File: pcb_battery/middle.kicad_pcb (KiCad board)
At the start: 2 copper layers, 100 x 29.9 mm, 7 parts, among them J1 BAT+, J2 BAT-, J3 TOP+, J4 BOT+, J5 TOP-, J6 BOT-

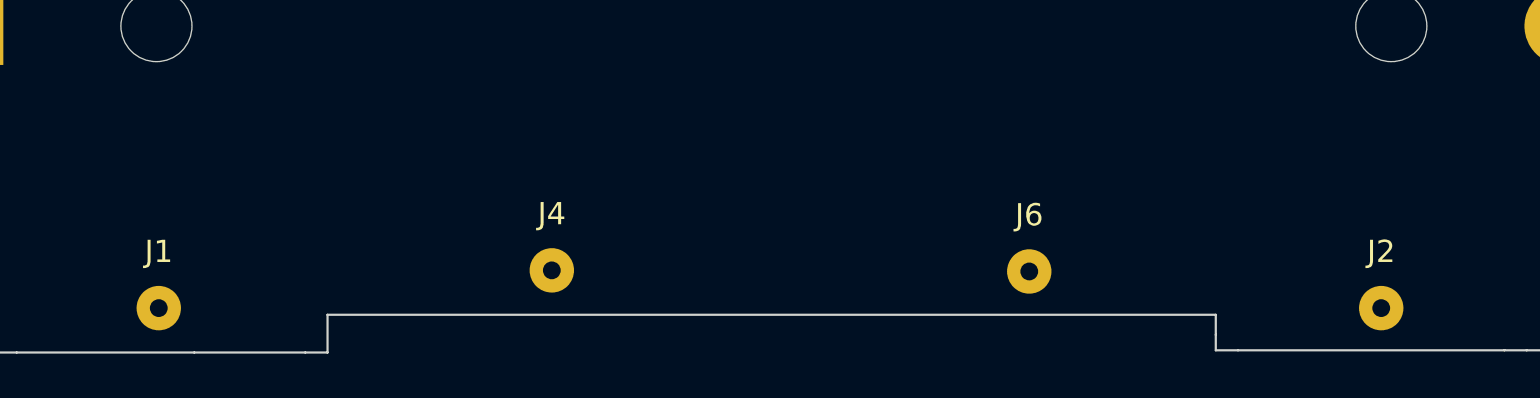
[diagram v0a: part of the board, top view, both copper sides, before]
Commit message: Add the bottom pcb.
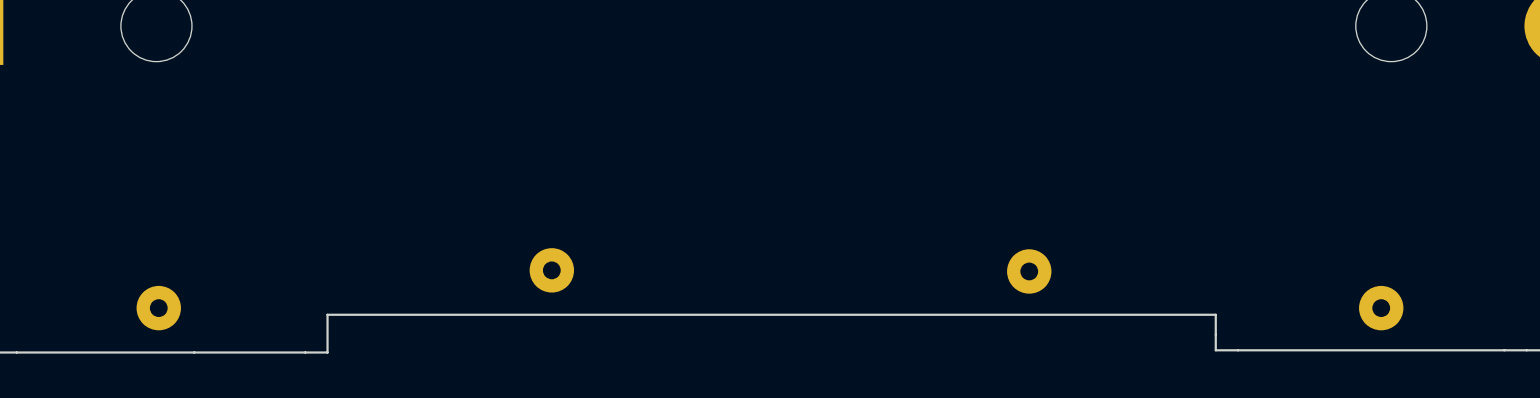
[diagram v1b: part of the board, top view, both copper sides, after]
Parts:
- J1, J2, J4, J6: moved to B.Cu
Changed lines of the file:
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@@
     (add_net "Net-(J5-Pad1)")
   )
-  (module Connector_Wire:SolderWirePad_1x01_Drill0.8mm (layer F.Cu)
+  (module Connector_Wire:SolderWirePad_1x01_Drill0.8mm (layer B.Cu)
     (at 11.6 -18.35)
     (descr "Wire solder connection")
     (tags connector)
     (attr virtual)
-    (fp_text reference J6 (at 0 -2.54) (layer F.SilkS)
-      (effects (font (size 1 1) (thickness 0.15)))
+    (fp_text reference J6 (at 3.7 0.3) (layer B.SilkS)
+      (effects (font (size 1 1) (thickness 0.15)) (justify mirror))
     )
-    (fp_text value BOT- (at 0 2.54) (layer F.Fab)
-      (effects (font (size 1 1) (thickness 0.15)))
+    (fp_text value BOT- (at -4.35 0.55) (layer B.Fab)
+      (effects (font (size 1 1) (thickness 0.15)) (justify mirror))
     )
-    (fp_line (start 1.5 1.5) (end -1.5 1.5) (layer F.CrtYd) (width 0.05))
-    (fp_line (start 1.5 1.5) (end 1.5 -1.5) (layer F.CrtYd) (width 0.05))
-    (fp_line (start -1.5 -1.5) (end -1.5 1.5) (layer F.CrtYd) (width 0.05))
-    (fp_line (start -1.5 -1.5) (end 1.5 -1.5) (layer F.CrtYd) (width 0.05))
-    (fp_text user %R (at 0 0) (layer F.Fab)
-      (effects (font (size 1 1) (thickness 0.15)))
+    (fp_line (start 1.5 -1.5) (end -1.5 -1.5) (layer B.CrtYd) (width 0.05))
+    (fp_line (start 1.5 -1.5) (end 1.5 1.5) (layer B.CrtYd) (width 0.05))
+    (fp_line (start -1.5 1.5) (end -1.5 -1.5) (layer B.CrtYd) (width 0.05))
+    (fp_line (start -1.5 1.5) (end 1.5 1.5) (layer B.CrtYd) (width 0.05))
+    (fp_text user %R (at 0 0) (layer B.Fab)
+      (effects (font (size 1 1) (thickness 0.15)) (justify mirror))
     )
     (pad 1 thru_hole circle (at 0 0) (size 1.99898 1.99898) (drill 0.8001) (layers *.Cu *.Mask)
@@
       (net 4 "Net-(J5-Pad1)"))
   )
-  (module Connector_Wire:SolderWirePad_1x01_Drill0.8mm (layer F.Cu)
+  (module Connector_Wire:SolderWirePad_1x01_Drill0.8mm (layer B.Cu)
     (at -9.9 -18.4)
     (descr "Wire solder connection")
     (tags connector)
     (attr virtual)
-    (fp_text reference J4 (at 0 -2.54) (layer F.SilkS)
-      (effects (font (size 1 1) (thickness 0.15)))
+    (fp_text reference J4 (at 3.6 0.4) (layer B.SilkS)
+      (effects (font (size 1 1) (thickness 0.15)) (justify mirror))
     )
-    (fp_text value BOT+ (at 0 2.54) (layer F.Fab)
-      (effects (font (size 1 1) (thickness 0.15)))
+    (fp_text value BOT+ (at -4 0.75) (layer B.Fab)
+      (effects (font (size 1 1) (thickness 0.15)) (justify mirror))
     )
-    (fp_line (start 1.5 1.5) (end -1.5 1.5) (layer F.CrtYd) (width 0.05))
-    (fp_line (start 1.5 1.5) (end 1.5 -1.5) (layer F.CrtYd) (width 0.05))
-    (fp_line (start -1.5 -1.5) (end -1.5 1.5) (layer F.CrtYd) (width 0.05))
-    (fp_line (start -1.5 -1.5) (end 1.5 -1.5) (layer F.CrtYd) (width 0.05))
-    (fp_text user %R (at 0 0) (layer F.Fab)
-      (effects (font (size 1 1) (thickness 0.15)))
+    (fp_line (start 1.5 -1.5) (end -1.5 -1.5) (layer B.CrtYd) (width 0.05))
+    (fp_line (start 1.5 -1.5) (end 1.5 1.5) (layer B.CrtYd) (width 0.05))
+    (fp_line (start -1.5 1.5) (end -1.5 -1.5) (layer B.CrtYd) (width 0.05))
+    (fp_line (start -1.5 1.5) (end 1.5 1.5) (layer B.CrtYd) (width 0.05))
+    (fp_text user %R (at 0 0) (layer B.Fab)
+      (effects (font (size 1 1) (thickness 0.15)) (justify mirror))
     )
     (pad 1 thru_hole circle (at 0 0) (size 1.99898 1.99898) (drill 0.8001) (layers *.Cu *.Mask)
@@
       (net 3 "Net-(J3-Pad1)"))
   )
-  (module Connector_Wire:SolderWirePad_1x01_Drill0.8mm (layer F.Cu)
+  (module Connector_Wire:SolderWirePad_1x01_Drill0.8mm (layer B.Cu)
     (at 27.45 -16.7)
     (descr "Wire solder connection")
     (tags connector)
     (attr virtual)
-    (fp_text reference J2 (at 0 -2.54) (layer F.SilkS)
-      (effects (font (size 1 1) (thickness 0.15)))
+    (fp_text reference J2 (at 0 2.54) (layer B.SilkS)
+      (effects (font (size 1 1) (thickness 0.15)) (justify mirror))
     )
-    (fp_text value BAT- (at 0 2.54) (layer F.Fab)
-      (effects (font (size 1 1) (thickness 0.15)))
+    (fp_text value BAT- (at 3.35 -0.2) (layer B.Fab)
+      (effects (font (size 1 1) (thickness 0.15)) (justify mirror))
     )
-    (fp_line (start 1.5 1.5) (end -1.5 1.5) (layer F.CrtYd) (width 0.05))
-    (fp_line (start 1.5 1.5) (end 1.5 -1.5) (layer F.CrtYd) (width 0.05))
-    (fp_line (start -1.5 -1.5) (end -1.5 1.5) (layer F.CrtYd) (width 0.05))
-    (fp_line (start -1.5 -1.5) (end 1.5 -1.5) (layer F.CrtYd) (width 0.05))
-    (fp_text user %R (at 0 0) (layer F.Fab)
-      (effects (font (size 1 1) (thickness 0.15)))
+    (fp_line (start 1.5 -1.5) (end -1.5 -1.5) (layer B.CrtYd) (width 0.05))
+    (fp_line (start 1.5 -1.5) (end 1.5 1.5) (layer B.CrtYd) (width 0.05))
+    (fp_line (start -1.5 1.5) (end -1.5 -1.5) (layer B.CrtYd) (width 0.05))
+    (fp_line (start -1.5 1.5) (end 1.5 1.5) (layer B.CrtYd) (width 0.05))
+    (fp_text user %R (at 0 0) (layer B.Fab)
+      (effects (font (size 1 1) (thickness 0.15)) (justify mirror))
     )
     (pad 1 thru_hole circle (at 0 0) (size 1.99898 1.99898) (drill 0.8001) (layers *.Cu *.Mask)
       (net 2 "Net-(BT1-Pad2)"))
   )
-  (module Connector_Wire:SolderWirePad_1x01_Drill0.8mm (layer F.Cu)
+  (module Connector_Wire:SolderWirePad_1x01_Drill0.8mm (layer B.Cu)
     (at -27.6 -16.7)
     (descr "Wire solder connection")
     (tags connector)
     (attr virtual)
-    (fp_text reference J1 (at 0 -2.54) (layer F.SilkS)
-      (effects (font (size 1 1) (thickness 0.15)))
+    (fp_text reference J1 (at -7.75 -0.7) (layer B.SilkS)
+      (effects (font (size 1 1) (thickness 0.15)) (justify mirror))
     )
-    (fp_text value BAT+ (at 0 2.54) (layer F.Fab)
-      (effects (font (size 1 1) (thickness 0.15)))
+    (fp_text value BAT+ (at 4.1 0.7) (layer B.Fab)
+      (effects (font (size 1 1) (thickness 0.15)) (justify mirror))
     )
-    (fp_line (start 1.5 1.5) (end -1.5 1.5) (layer F.CrtYd) (width 0.05))
-    (fp_line (start 1.5 1.5) (end 1.5 -1.5) (layer F.CrtYd) (width 0.05))
-    (fp_line (start -1.5 -1.5) (end -1.5 1.5) (layer F.CrtYd) (width 0.05))
-    (fp_line (start -1.5 -1.5) (end 1.5 -1.5) (layer F.CrtYd) (width 0.05))
-    (fp_text user %R (at 0 0) (layer F.Fab)
-      (effects (font (size 1 1) (thickness 0.15)))
+    (fp_line (start 1.5 -1.5) (end -1.5 -1.5) (layer B.CrtYd) (width 0.05))
+    (fp_line (start 1.5 -1.5) (end 1.5 1.5) (layer B.CrtYd) (width 0.05))
+    (fp_line (start -1.5 1.5) (end -1.5 -1.5) (layer B.CrtYd) (width 0.05))
+    (fp_line (start -1.5 1.5) (end 1.5 1.5) (layer B.CrtYd) (width 0.05))
+    (fp_text user %R (at 0 0) (layer B.Fab)
+      (effects (font (size 1 1) (thickness 0.15)) (justify mirror))
     )
     (pad 1 thru_hole circle (at 0 0) (size 1.99898 1.99898) (drill 0.8001) (layers *.Cu *.Mask)

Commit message: All 3 parts done
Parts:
- moved J6 1.60 mm to (10.0, -18.4)
- moved J4 0.10 mm to (-10.0, -18.4)
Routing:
- net Net-(J3-Pad1): track 0.00 -> 34.8 mm
- net Net-(J5-Pad1): track 0.00 -> 34.7 mm
- net Net-(BT1-Pad1): track 0.00 -> 19.4 mm
- net Net-(BT1-Pad2): track 0.00 -> 19.2 mm
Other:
- net class Default: trace_width 0.25 -> 0.3
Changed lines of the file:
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@@
     (thickness 1.6)
     (drawings 102)
-    (tracks 0)
+    (tracks 12)
     (zones 0)
     (modules 7)
@@
   )
   (setup
-    (last_trace_width 0.25)
+    (last_trace_width 0.3)
     (trace_clearance 0.2)
     (zone_clearance 0.508)
@@
     (mod_text_size 1 1)
     (mod_text_width 0.15)
-    (pad_size 18 3)
+    (pad_size 15 2.5)
     (pad_drill 0)
     (pad_to_mask_clearance 0.2)
@@
   (net_class Default "This is the default net class."
     (clearance 0.2)
-    (trace_width 0.25)
+    (trace_width 0.3)
     (via_dia 0.6)
     (via_drill 0.4)
@@
   )
   (module Connector_Wire:SolderWirePad_1x01_Drill0.8mm (layer B.Cu)
-    (at 11.6 -18.35)
-    (descr "Wire solder connection")
-    (tags connector)
-    (attr virtual)
-    (fp_text reference J6 (at 3.7 0.3) (layer B.SilkS)
-      (effects (font (size 1 1) (thickness 0.15)) (justify mirror))
-    )
-    (fp_text value BOT- (at -4.35 0.55) (layer B.Fab)
-      (effects (font (size 1 1) (thickness 0.15)) (justify mirror))
-    )
-    (fp_line (start 1.5 -1.5) (end -1.5 -1.5) (layer B.CrtYd) (width 0.05))
-    (fp_line (start 1.5 -1.5) (end 1.5 1.5) (layer B.CrtYd) (width 0.05))
-    (fp_line (start -1.5 1.5) (end -1.5 -1.5) (layer B.CrtYd) (width 0.05))
-    (fp_line (start -1.5 1.5) (end 1.5 1.5) (layer B.CrtYd) (width 0.05))
-    (fp_text user %R (at 0 0) (layer B.Fab)
-      (effects (font (size 1 1) (thickness 0.15)) (justify mirror))
-    )
-    (pad 1 thru_hole circle (at 0 0) (size 1.99898 1.99898) (drill 0.8001) (layers *.Cu *.Mask)
+    (at 10 -18.35)
+    (descr "Wire solder connection")
+    (tags connector)
+    (attr virtual)
+    (fp_text reference J6 (at 9 0.35) (layer B.SilkS)
+      (effects (font (size 1 1) (thickness 0.15)) (justify mirror))
+    )
+    (fp_text value BOT- (at 0 -2.65) (layer B.SilkS)
+      (effects (font (size 1 1) (thickness 0.15)) (justify mirror))
+    )
+    (fp_line (start 1.5 -1.5) (end -1.5 -1.5) (layer B.CrtYd) (width 0.05))
+    (fp_line (start 1.5 -1.5) (end 1.5 1.5) (layer B.CrtYd) (width 0.05))
+    (fp_line (start -1.5 1.5) (end -1.5 -1.5) (layer B.CrtYd) (width 0.05))
+    (fp_line (start -1.5 1.5) (end 1.5 1.5) (layer B.CrtYd) (width 0.05))
+    (fp_text user %R (at 0 0) (layer B.Fab)
+      (effects (font (size 1 1) (thickness 0.15)) (justify mirror))
+    )
+    (pad 1 smd oval (at 0 0) (size 15 2.5) (layers B.Cu B.Paste B.Mask)
       (net 4 "Net-(J5-Pad1)"))
   )
@@
       (effects (font (size 1 1) (thickness 0.15)) (justify mirror))
     )
-    (fp_text value TOP- (at 0 -2.54) (layer B.Fab)
+    (fp_text value TOP- (at -12.75 1.05) (layer B.SilkS)
       (effects (font (size 1 1) (thickness 0.15)) (justify mirror))
     )
@@
   )
   (module Connector_Wire:SolderWirePad_1x01_Drill0.8mm (layer B.Cu)
-    (at -9.9 -18.4)
-    (descr "Wire solder connection")
-    (tags connector)
-    (attr virtual)
-    (fp_text reference J4 (at 3.6 0.4) (layer B.SilkS)
-      (effects (font (size 1 1) (thickness 0.15)) (justify mirror))
-    )
-    (fp_text value BOT+ (at -4 0.75) (layer B.Fab)
-      (effects (font (size 1 1) (thickness 0.15)) (justify mirror))
-    )
-    (fp_line (start 1.5 -1.5) (end -1.5 -1.5) (layer B.CrtYd) (width 0.05))
-    (fp_line (start 1.5 -1.5) (end 1.5 1.5) (layer B.CrtYd) (width 0.05))
-    (fp_line (start -1.5 1.5) (end -1.5 -1.5) (layer B.CrtYd) (width 0.05))
-    (fp_line (start -1.5 1.5) (end 1.5 1.5) (layer B.CrtYd) (width 0.05))
-    (fp_text user %R (at 0 0) (layer B.Fab)
-      (effects (font (size 1 1) (thickness 0.15)) (justify mirror))
-    )
-    (pad 1 thru_hole circle (at 0 0) (size 1.99898 1.99898) (drill 0.8001) (layers *.Cu *.Mask)
+    (at -10 -18.4)
+    (descr "Wire solder connection")
+    (tags connector)
+    (attr virtual)
+    (fp_text reference J4 (at -9 0.4) (layer B.SilkS)
+      (effects (font (size 1 1) (thickness 0.15)) (justify mirror))
+    )
+    (fp_text value BOT+ (at 0 -2.6) (layer B.SilkS)
+      (effects (font (size 1 1) (thickness 0.15)) (justify mirror))
+    )
+    (fp_line (start 1.5 -1.5) (end -1.5 -1.5) (layer B.CrtYd) (width 0.05))
+    (fp_line (start 1.5 -1.5) (end 1.5 1.5) (layer B.CrtYd) (width 0.05))
+    (fp_line (start -1.5 1.5) (end -1.5 -1.5) (layer B.CrtYd) (width 0.05))
+    (fp_line (start -1.5 1.5) (end 1.5 1.5) (layer B.CrtYd) (width 0.05))
+    (fp_text user %R (at 0 0) (layer B.Fab)
+      (effects (font (size 1 1) (thickness 0.15)) (justify mirror))
+    )
+    (pad 1 smd oval (at 0 0) (size 15 2.5) (layers B.Cu B.Paste B.Mask)
       (net 3 "Net-(J3-Pad1)"))
   )
@@
       (effects (font (size 1 1) (thickness 0.15)) (justify mirror))
     )
-    (fp_text value TOP+ (at 0 -2.54) (layer B.Fab)
+    (fp_text value TOP+ (at -12.85 1.55) (layer B.SilkS)
       (effects (font (size 1 1) (thickness 0.15)) (justify mirror))
     )
@@
     (tags connector)
     (attr virtual)
-    (fp_text reference J2 (at 0 2.54) (layer B.SilkS)
-      (effects (font (size 1 1) (thickness 0.15)) (justify mirror))
-    )
-    (fp_text value BAT- (at 3.35 -0.2) (layer B.Fab)
-      (effects (font (size 1 1) (thickness 0.15)) (justify mirror))
-    )
-    (fp_line (start 1.5 -1.5) (end -1.5 -1.5) (layer B.CrtYd) (width 0.05))
-    (fp_line (start 1.5 -1.5) (end 1.5 1.5) (layer B.CrtYd) (width 0.05))
-    (fp_line (start -1.5 1.5) (end -1.5 -1.5) (layer B.CrtYd) (width 0.05))
-    (fp_line (start -1.5 1.5) (end 1.5 1.5) (layer B.CrtYd) (width 0.05))
-    (fp_text user %R (at 0 0) (layer B.Fab)
-      (effects (font (size 1 1) (thickness 0.15)) (justify mirror))
-    )
-    (pad 1 thru_hole circle (at 0 0) (size 1.99898 1.99898) (drill 0.8001) (layers *.Cu *.Mask)
+    (fp_text reference J2 (at 8.55 -0.8) (layer B.SilkS)
+      (effects (font (size 1 1) (thickness 0.15)) (justify mirror))
+    )
+    (fp_text value BAT- (at 11.55 -0.8) (layer B.SilkS)
+      (effects (font (size 1 1) (thickness 0.15)) (justify mirror))
+    )
+    (fp_line (start 1.5 -1.5) (end -1.5 -1.5) (layer B.CrtYd) (width 0.05))
+    (fp_line (start 1.5 -1.5) (end 1.5 1.5) (layer B.CrtYd) (width 0.05))
+    (fp_line (start -1.5 1.5) (end -1.5 -1.5) (layer B.CrtYd) (width 0.05))
+    (fp_line (start -1.5 1.5) (end 1.5 1.5) (layer B.CrtYd) (width 0.05))
+    (fp_text user %R (at 0 0) (layer B.Fab)
+      (effects (font (size 1 1) (thickness 0.15)) (justify mirror))
+    )
+    (pad 1 smd oval (at 0 0) (size 13 2.5) (layers B.Cu B.Paste B.Mask)
       (net 2 "Net-(BT1-Pad2)"))
   )
@@
     (tags connector)
     (attr virtual)
-    (fp_text reference J1 (at -7.75 -0.7) (layer B.SilkS)
-      (effects (font (size 1 1) (thickness 0.15)) (justify mirror))
-    )
-    (fp_text value BAT+ (at 4.1 0.7) (layer B.Fab)
-      (effects (font (size 1 1) (thickness 0.15)) (justify mirror))
-    )
-    (fp_line (start 1.5 -1.5) (end -1.5 -1.5) (layer B.CrtYd) (width 0.05))
-    (fp_line (start 1.5 -1.5) (end 1.5 1.5) (layer B.CrtYd) (width 0.05))
-    (fp_line (start -1.5 1.5) (end -1.5 -1.5) (layer B.CrtYd) (width 0.05))
-    (fp_line (start -1.5 1.5) (end 1.5 1.5) (layer B.CrtYd) (width 0.05))
-    (fp_text user %R (at 0 0) (layer B.Fab)
-      (effects (font (size 1 1) (thickness 0.15)) (justify mirror))
-    )
-    (pad 1 thru_hole circle (at 0 0) (size 1.99898 1.99898) (drill 0.8001) (layers *.Cu *.Mask)
+    (fp_text reference J1 (at -8.4 -0.8) (layer B.SilkS)
+      (effects (font (size 1 1) (thickness 0.15)) (justify mirror))
+    )
+    (fp_text value BAT+ (at -11.9 -0.8) (layer B.SilkS)
+      (effects (font (size 1 1) (thickness 0.15)) (justify mirror))
+    )
+    (fp_line (start 1.5 -1.5) (end -1.5 -1.5) (layer B.CrtYd) (width 0.05))
+    (fp_line (start 1.5 -1.5) (end 1.5 1.5) (layer B.CrtYd) (width 0.05))
+    (fp_line (start -1.5 1.5) (end -1.5 -1.5) (layer B.CrtYd) (width 0.05))
+    (fp_line (start -1.5 1.5) (end 1.5 1.5) (layer B.CrtYd) (width 0.05))
+    (fp_text user %R (at 0 0) (layer B.Fab)
+      (effects (font (size 1 1) (thickness 0.15)) (justify mirror))
+    )
+    (pad 1 smd oval (at 0 0) (size 13 2.5) (layers B.Cu B.Paste B.Mask)
       (net 1 "Net-(BT1-Pad1)"))
   )
@@
   (gr_line (start -45.966545 -42.995933) (end -45.966593 -42.99593) (layer Edge.Cuts) (width 0.1))
   (gr_line (start -45.966593 -42.99593) (end -45.966593 -42.99593) (layer Edge.Cuts) (width 0.1))
+  (segment (start -32.85 -16.7) (end -27.6 -16.7) (width 0.3) (layer B.Cu) (net 1))
+  (segment (start -36.35 -20.2) (end -32.85 -16.7) (width 0.3) (layer B.Cu) (net 1))
+  (segment (start -36.35 -29.4) (end -36.35 -20.2) (width 0.3) (layer B.Cu) (net 1))
+  (segment (start 32.7 -16.7) (end 27.45 -16.7) (width 0.3) (layer B.Cu) (net 2))
+  (segment (start 35.65 -19.65) (end 32.7 -16.7) (width 0.3) (layer B.Cu) (net 2))
+  (segment (start 35.65 -29.4) (end 35.65 -19.65) (width 0.3) (layer B.Cu) (net 2))
+  (segment (start -17.65 -42.55) (end -25.15 -42.55) (width 0.3) (layer B.Cu) (net 3))
+  (segment (start -10 -34.9) (end -17.65 -42.55) (width 0.3) (layer B.Cu) (net 3))
+  (segment (start -10 -18.4) (end -10 -34.9) (width 0.3) (layer B.Cu) (net 3))
+  (segment (start 17.25 -42.55) (end 24.75 -42.55) (width 0.3) (layer B.Cu) (net 4))
+  (segment (start 10 -35.3) (end 17.25 -42.55) (width 0.3) (layer B.Cu) (net 4))
+  (segment (start 10 -18.35) (end 10 -35.3) (width 0.3) (layer B.Cu) (net 4))
 )

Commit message: Few more small improvements.
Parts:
- added Ref**: Val**, logos:josef_adamcik_20mm_cu_mask, F.Cu at (0.30, -25.9)
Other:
- board text added: "@josefadamcik"
- board text added: "https://josef-adamcik.cz"
